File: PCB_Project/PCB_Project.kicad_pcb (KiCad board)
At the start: 4 copper layers, 53 x 30 mm, 39 parts, among them J1 Power Connector, J2 ZE27-O3, J3 i2c1, J4 i2c2, J5 SPI1, J6 SPI2, Q1 MMBT2222A, Q2 MMBT2222A

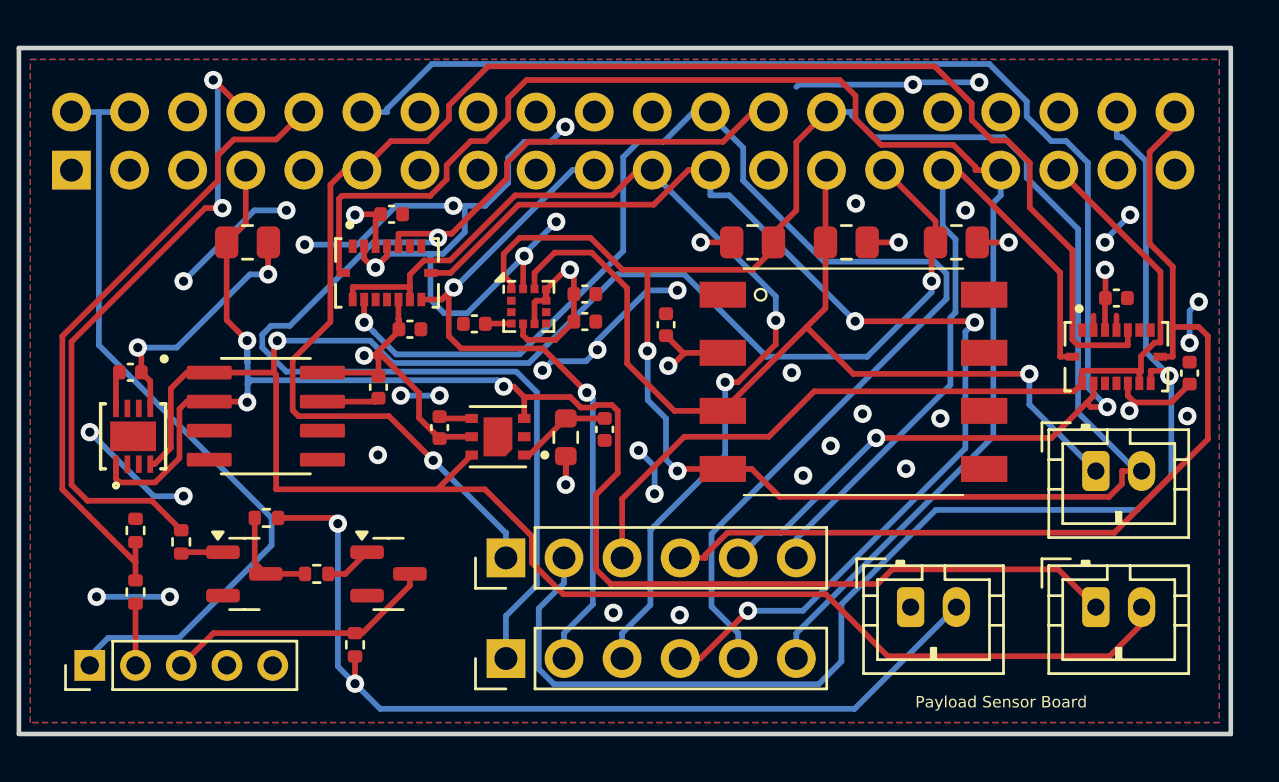
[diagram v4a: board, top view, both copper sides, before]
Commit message: added fabs and fixed i2c loop
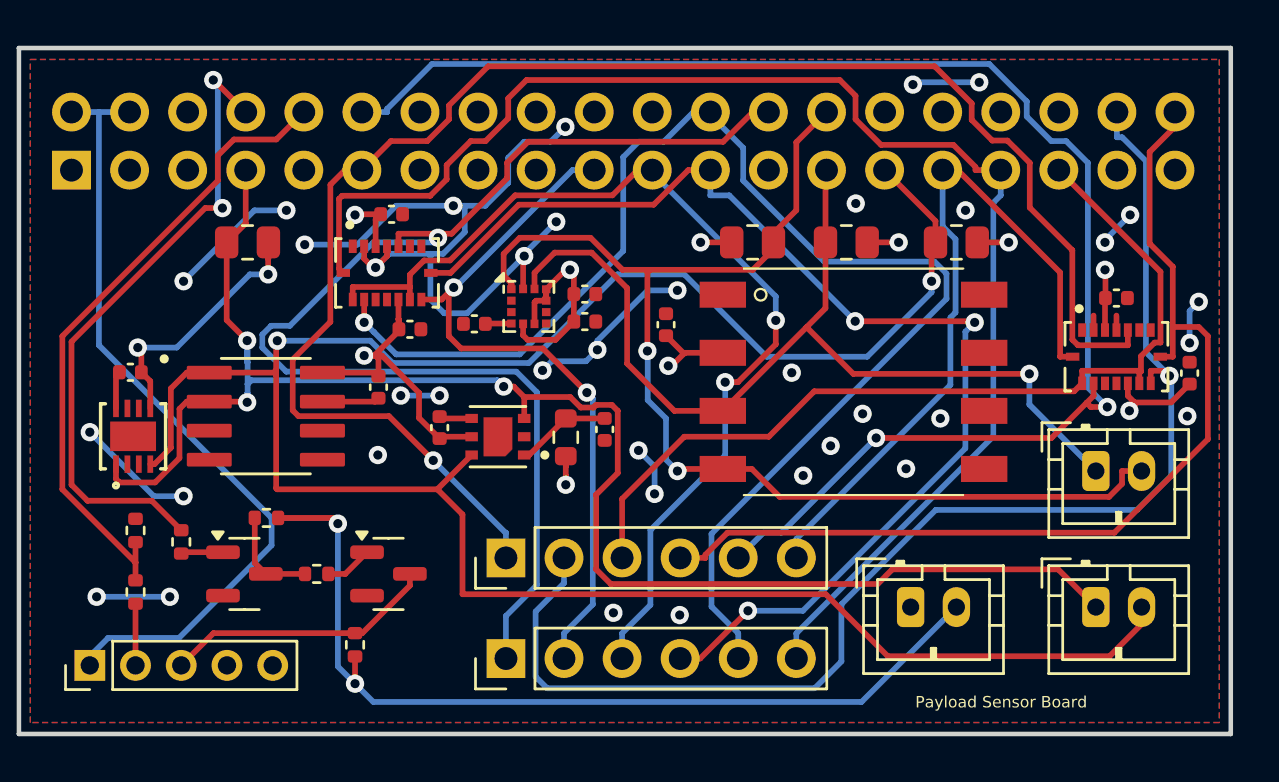
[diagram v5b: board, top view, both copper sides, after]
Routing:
- net I2C_SCL_1: track 78.3 -> 52.8 mm
- net GND: track 77.4 -> 72.3 mm
- net +3V3: track 55.4 -> 53.4 mm
- net I2C_SCL_2: track 100.3 -> 101.9 mm
- net MOSI_2: track 57.4 -> 57.9 mm

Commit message: power baby
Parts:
- removed R22, R23, R24, R25, R27: 1k, Resistor_SMD:R_0402_1005Metric
- removed R26: 2k, Resistor_SMD:R_0402_1005Metric
- added 11: LM22673MRE-5.0/NOPB, Transistor_Power:MRA08B, F.Cu at (89.6, 22.3)
- added C14: 6.8uF, Capacitor_SMD:C_1206_3216Metric, F.Cu at (96.2, 22.2)
- added C15: 1uF, Capacitor_SMD:C_0603_1608Metric, F.Cu at (93.0, 26.5)
- added D2: LED_Small, LED_SMD:LED_0805_2012Metric, F.Cu at (189.7, 84.3)
- added D3: LED_Small, LED_SMD:LED_0805_2012Metric, F.Cu at (111.8, 79.7)
- added D4: LED_Small, LED_SMD:LED_0805_2012Metric, F.Cu at (114.6, 79.7)
- added D5: LED_Small, LED_SMD:LED_0805_2012Metric, F.Cu at (117.8, 79.7)
- added D6: LED_Small, LED_SMD:LED_0805_2012Metric, F.Cu at (108.5, 79.7)
- added D7: LED_Small, LED_SMD:LED_0805_2012Metric, F.Cu at (127.8, 79.8)
- added J10: ZE27-O3, Connector_PinHeader_2.00mm:PinHeader_1x05_P2.00mm_Vertical, F.Cu at (157.1, 43.9)
- added J7: m2, Connector_JST:JST_PH_B2B-PH-K_1x02_P2.00mm_Vertical, F.Cu at (85.0, 170.2)
- added J8: m3, Connector_JST:JST_PH_B2B-PH-K_1x02_P2.00mm_Vertical, F.Cu at (96.5, 170.1)
- added J9: m4, Connector_JST:JST_PH_B2B-PH-K_1x02_P2.00mm_Vertical, F.Cu at (53.0, 170.2)
- added R10: 310, Resistor_SMD:R_0402_1005Metric, F.Cu at (185.3, 78.8)
- added R11: 310, Resistor_SMD:R_0402_1005Metric, F.Cu at (185.3, 80.8)
- added R12: 310, Resistor_SMD:R_0402_1005Metric, F.Cu at (185.3, 82.8)
- added R13: 430, Resistor_SMD:R_0402_1005Metric, F.Cu at (185.3, 84.8)
- added R14: 110, Resistor_SMD:R_0402_1005Metric, F.Cu at (161.1, 39.7)
- added R15: 1k, Resistor_SMD:R_0402_1005Metric, F.Cu at (162.4, 39.7)
- added R16: 1k, Resistor_SMD:R_0402_1005Metric, F.Cu at (164.4, 37.2)
- added R17: 1k, Resistor_SMD:R_0402_1005Metric, F.Cu at (162.1, 33.0)
- added R18: 1k, Resistor_SMD:R_0402_1005Metric, F.Cu at (157.9, 38.2)
- added R19: 2k, Resistor_SMD:R_0402_1005Metric, F.Cu at (157.9, 40.7)
- added R20: 1k, Resistor_SMD:R_0402_1005Metric, F.Cu at (111.8, 82.9)
- added R6: 1k, Resistor_SMD:R_0603_1608Metric, F.Cu at (105.3, 17.1)
- added R7: 45, Resistor_SMD:R_0603_1608Metric, F.Cu at (105.3, 19.6)
- added R9: 310, Resistor_SMD:R_0402_1005Metric, F.Cu at (185.3, 76.8)
- added U9: TPS7A5701RTER, Package_TO_SOT_SMD:WQFN16_RTE_TEX, F.Cu at (190.3, 90.8)
- C12: value 100nF -> 10nF; footprint Capacitor_SMD:C_0402_1005Metric -> Capacitor_SMD:C_0603_1608Metric
- C3: value 1µF -> 100nF
- C4: value 100nF -> 1µF
- C8: value 0.1µF -> 100nF
- J1: value Power Connector -> i2c2
- J2: value ZE27-O3 -> i2c1; footprint Connector_PinHeader_2.00mm:PinHeader_1x05_P2.00mm_Vertical -> Connector_JST:JST_PH_B2B-PH-K_1x02_P2.00mm_Vertical
- J3: value i2c1 -> SPI1; footprint Connector_JST:JST_PH_B2B-PH-K_1x02_P2.00mm_Vertical -> Connector_PinHeader_2.54mm:PinHeader_1x06_P2.54mm_Vertical
- J4: value i2c2 -> SPI2; footprint Connector_JST:JST_PH_B2B-PH-K_1x02_P2.00mm_Vertical -> Connector_PinHeader_2.54mm:PinHeader_1x06_P2.54mm_Vertical
- J5: value SPI1 -> Power Connector; footprint Connector_PinHeader_2.54mm:PinHeader_1x06_P2.54mm_Vertical -> Connector_JST:JST_PH_B2B-PH-K_1x02_P2.00mm_Vertical
- J6: value SPI2 -> m1; footprint Connector_PinHeader_2.54mm:PinHeader_1x06_P2.54mm_Vertical -> Connector_JST:JST_PH_B2B-PH-K_1x02_P2.00mm_Vertical
- U2: footprint Package_LGA:LGA-12_2x2mm_P0.5mm -> Sensor:XDCR_SGP41-D-R4
- U3: footprint Sensor:XDCR_SGP41-D-R4 -> Package_LGA:LGA-12_2x2mm_P0.5mm
- moved C7 147.0 mm to (251.9, 47.1)
- moved U6 147.0 mm to (247.0, 48.4)
- moved C5 131.4 mm to (227.7, 21.9), turned to 90 degrees
- moved R5 123.1 mm to (221.8, 19.4), turned to -90 degrees
- moved U2 123.0 mm to (224.7, 21.5)
- moved C4 122.3 mm to (220.2, 20.0), turned to 90 degrees
- moved U3 111.1 mm to (216.3, 40.2)
- moved C3 108.3 mm to (217.0, 37.8), turned to 90 degrees
- moved C1 105.4 mm to (215.2, 37.0), turned to 180 degrees
- moved C2 105.4 mm to (215.2, 38.2), turned to 180 degrees
- moved J2 105.3 mm to (190.5, 46.8)
- moved Q2 96.7 mm to (199.7, 82.8)
- moved J6 92.4 mm to (62.5, 170.4), turned to 0 degrees
- moved Q1 90.9 mm to (199.7, 78.2)
- moved J5 90.6 mm to (73.5, 170.4), turned to 0 degrees
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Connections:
- C12 pad 1: +3V3 -> Net-(11-BOOT)
- C12 pad 2: GND -> Net-(11-SW)
- C3 pad 1: Net-(U3-VDD) -> Net-(U3-C1)
- C4 pad 1: Net-(U2-C1) -> Net-(U2-VDD)
- C6 pad 1: GND -> +3V3
- C6 pad 2: +3V3 -> GND
- J1 pad 1: GND -> I2C_SDA_2
- J1 pad 2: +5V -> I2C_SCL_2
- J2 pad 1: +5V -> I2C_SDA_1
- J2 pad 2: Pi_RX_5V -> I2C_SCL_1
- J3 pad 1: I2C_SDA_1 -> CSB_Gryo_BMI088_2
- J3 pad 2: I2C_SCL_1 -> MOSI_2
- J4 pad 1: I2C_SDA_2 -> CSB_Gryo_BMI088_1
- J4 pad 2: I2C_SCL_2 -> MOSI_1
- J5 pad 1: CSB_Gryo_BMI088_2 -> GND
- J5 pad 2: MOSI_2 -> BATTV
- J6 pad 1: CSB_Gryo_BMI088_1 -> GND
- J6 pad 2: MOSI_1 -> S1
- R5 pad 2: Net-(U3-VDD) -> Net-(U2-VDD)
- U2 pad 1: I2C_SCL_1 -> Net-(U2-VDD)
- U2 pad 3: GND -> I2C_SDA_2
- U2 pad 4: Net-(U2-C1) -> GND
- U2 pad 6: +3V3 -> I2C_SCL_2
- U2 pad 7: unconnected-(U2-Int-Pad7) -> GND
- U3 pad 1: Net-(U3-VDD) -> I2C_SCL_1
- U3 pad 3: I2C_SDA_2 -> GND
- U3 pad 4: GND -> Net-(U3-C1)
- U3 pad 6: I2C_SCL_2 -> +3V3
- U3 pad 7: GND -> unconnected-(U3-Int-Pad7)
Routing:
- net I2C_SCL_2: track 101.9 -> 0.00 mm, vias 2 -> 0
- net +5V: track 77.7 -> 0.00 mm, vias 2 -> 0
- net GND: track 72.3 -> 0.00 mm, vias 31 -> 0
- net CSB_Gryo_BMI088_2: track 70.2 -> 0.00 mm, vias 1 -> 0
- net I2C_SDA_2: track 69.7 -> 0.00 mm, vias 3 -> 0
- net CSB_Accel_BMI088_2: track 65.9 -> 0.00 mm, vias 2 -> 0
- net BMI088_INT1_1: track 62.7 -> 0.00 mm
- net CSB_Accel_BMI088_1: track 59.3 -> 0.00 mm, vias 1 -> 0
- net MOSI_2: track 57.9 -> 0.00 mm, vias 1 -> 0
- net CSB_Gryo_BMI088_1: track 54.5 -> 0.00 mm, vias 1 -> 0
- net +3V3: track 53.4 -> 0.00 mm, vias 18 -> 0
- net I2C_SCL_1: track 52.8 -> 0.00 mm, vias 2 -> 0
- net SCK_1: track 51.0 -> 0.00 mm, vias 3 -> 0
- net SCK_2: track 43.6 -> 0.00 mm
- net MISO_1: track 43.6 -> 0.00 mm, vias 2 -> 0
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- added copper zone on B.Cu, net BATTV
- removed copper zone on B.Cu, net +3V3
- removed copper zone on In2.Cu, net +3V3
- removed copper zone on F.Cu, net GND
- removed copper zone on In1.Cu, net GND
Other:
- board size 53 x 30 mm -> 70 x 70 mm
- board text added: "1"
- board text added: "2"
- board text added: "3"
- board text added: "4"
- board text added: "5V"
- board text added: "BATT"
- board text added: "STARR"
- board text removed: "Payload Sensor Board"

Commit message: finally
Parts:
- removed 11: LM22673MRE-5.0/NOPB, Transistor_Power:MRA08B
- removed J7: m2, Connector_JST:JST_PH_B2B-PH-K_1x02_P2.00mm_Vertical
- removed J8: m3, Connector_JST:JST_PH_B2B-PH-K_1x02_P2.00mm_Vertical
- removed J9: m4, Connector_JST:JST_PH_B2B-PH-K_1x02_P2.00mm_Vertical
- removed R10, R11: 310, Resistor_SMD:R_0402_1005Metric
- removed R14: 110, Resistor_SMD:R_0402_1005Metric
- removed U9: TPS7A5701RTER, Package_TO_SOT_SMD:WQFN16_RTE_TEX
- added 111: LM22673MRE-5.0/NOPB, Transistor_Power:MRA08B, F.Cu at (112.0, 85.9)
- added 1111: LM22673MRE-5.0/NOPB, Transistor_Power:MRA08B, B.Cu at (102.6, 85.6)
- added 11111: LM22673MRE-5.0/NOPB, Transistor_Power:MRA08B, B.Cu at (122.4, 85.7)
- added 11112: LM22673MRE-5.0/NOPB, Transistor_Power:MRA08B, F.Cu at (146.6, 97.4)
- added 11113: LM22673MRE-5.0/NOPB, Transistor_Power:MRA08B, B.Cu at (140.9, 85.7)
- added 11114: LM22673MRE-5.0/NOPB, Transistor_Power:MRA08B, B.Cu at (161.3, 85.8)
- added C13: 100uF, Capacitor_SMD:CP_WCAP-PSHP, B.Cu at (108.5, 72.8)
- added C16: 100uF, Capacitor_SMD:CP_WCAP-PSHP, F.Cu at (113.8, 97.5)
- added C17: 6.8uF, Capacitor_SMD:C_1206_3216Metric, F.Cu at (112.0, 91.2)
- added C18: 1uF, Capacitor_SMD:C_0603_1608Metric, B.Cu at (98.4, 82.3)
- added C19: 120uF, Capacitor_SMD:CP_Elec_10x12.5, B.Cu at (113.2, 96.0)
- added C20: 1uF, Capacitor_SMD:C_0603_1608Metric, F.Cu at (107.8, 89.0)
- added C21: 120uF, Capacitor_SMD:CP_Elec_10x12.5, F.Cu at (119.5, 76.0)
- added C22: 10nF, Capacitor_SMD:C_0603_1608Metric, B.Cu at (126.5, 85.8)
- added C23: 100uF, Capacitor_SMD:CP_WCAP-PSHP, B.Cu at (124.0, 72.0)
- added C24: 6.8uF, Capacitor_SMD:C_1206_3216Metric, B.Cu at (122.4, 80.2)
- added C25: 1uF, Capacitor_SMD:C_0603_1608Metric, B.Cu at (118.2, 82.5)
- added C26: 120uF, Capacitor_SMD:CP_Elec_10x12.5, B.Cu at (132.4, 95.2)
- added C27: 10nF, Capacitor_SMD:C_0603_1608Metric, F.Cu at (146.7, 93.5)
- added C28: 100uF, Capacitor_SMD:CP_WCAP-PSHP, F.Cu at (161.0, 94.8)
- added C29: 6.8uF, Capacitor_SMD:C_1206_3216Metric, F.Cu at (152.0, 97.2)
- added C30: 1uF, Capacitor_SMD:C_0603_1608Metric, F.Cu at (149.8, 101.5)
- added C31: 120uF, Capacitor_SMD:CP_Elec_10x12.5, F.Cu at (137.2, 88.8)
- added C32: 10nF, Capacitor_SMD:C_0603_1608Metric, B.Cu at (145.3, 85.8)
- added C33: 100uF, Capacitor_SMD:CP_WCAP-PSHP, B.Cu at (147.3, 72.0)
- added C34: 6.8uF, Capacitor_SMD:C_1206_3216Metric, B.Cu at (141.0, 80.3)
- added C35: 1uF, Capacitor_SMD:C_0603_1608Metric, B.Cu at (136.8, 82.5)
- added C36: 120uF, Capacitor_SMD:CP_Elec_10x12.5, B.Cu at (151.2, 95.3)
- added C37: 10nF, Capacitor_SMD:C_0603_1608Metric, B.Cu at (165.6, 85.7)
- added C38: 100uF, Capacitor_SMD:CP_WCAP-PSHP, B.Cu at (164.2, 71.2)
- added C39: 6.8uF, Capacitor_SMD:C_1206_3216Metric, B.Cu at (161.3, 80.3)
- added C40: 1uF, Capacitor_SMD:C_0603_1608Metric, B.Cu at (157.1, 82.5)
- added C41: 120uF, Capacitor_SMD:CP_Elec_10x12.5, B.Cu at (171.5, 95.3)
- added D1: 60V, 5A, Diode_SMD:D_PowerDI-5, B.Cu at (112.9, 79.6)
- added D10: 60V, 5A, Diode_SMD:D_PowerDI-5, B.Cu at (171.6, 79.2)
- added D11: LED_Small, Diode_SMD:D_0603_1608Metric, F.Cu at (160.2, 73.2)
- added D12: LED_Small, Diode_SMD:D_0603_1608Metric, F.Cu at (157.2, 73.2)
- added D13: LED_Small, Diode_SMD:D_0603_1608Metric, F.Cu at (154.0, 73.2)
- added D8: LED_Small, Diode_SMD:D_0603_1608Metric, F.Cu at (166.2, 73.2)
- added D9: LED_Small, Diode_SMD:D_0603_1608Metric, F.Cu at (163.2, 73.2)
- added H1: MountingHole_Pad, MountingHole:MountingHole_2.5mm_Pad, F.Cu at (99.6, 64.2)
- added H2: MountingHole_Pad, MountingHole:MountingHole_2.5mm_Pad, F.Cu at (157.6, 64.2)
- added H3: MountingHole_Pad, MountingHole:MountingHole_2.5mm_Pad, F.Cu at (99.6, 106.3)
- added H4: MountingHole_Pad, MountingHole:MountingHole_2.5mm_Pad, F.Cu at (157.6, 106.3)
- added J11: ZE27-O3, Connector_PinHeader_2.00mm:PinHeader_1x05_P2.00mm_Vertical, F.Cu at (98.8, 80.0)
- added J12: Conn_01x03_Socket, Connector_JST:JST_PH_B3B-PH-K_1x03_P2.00mm_Vertical, F.Cu at (105.8, 105.7)
- added J13: Conn_01x03_Socket, Connector_JST:JST_PH_B3B-PH-K_1x03_P2.00mm_Vertical, F.Cu at (138.8, 105.7)
- added J14: Conn_01x03_Socket, Connector_JST:JST_PH_B3B-PH-K_1x03_P2.00mm_Vertical, F.Cu at (148.1, 105.7)
- added L1: 6uH, Inductor_SMD:L_6.7x6.7mm, B.Cu at (111.5, 85.2)
- added L2: 6uH, Inductor_SMD:L_6.7x6.7mm, F.Cu at (120.5, 86.0)
- added L3: 6uH, Inductor_SMD:L_6.7x6.7mm, B.Cu at (131.0, 85.5)
- added L4: 6uH, Inductor_SMD:L_6.7x6.7mm, F.Cu at (147.0, 89.0)
- added L5: 6uH, Inductor_SMD:L_6.7x6.7mm, B.Cu at (150.0, 85.2)
- added L6: 6uH, Inductor_SMD:L_6.7x6.7mm, B.Cu at (170.3, 85.8)
- added R21: 1k, Resistor_SMD:R_0402_1005Metric, F.Cu at (101.8, 76.0)
- added R22: 1k, Resistor_SMD:R_0402_1005Metric, F.Cu at (105.7, 76.2)
- added R23: 1k, Resistor_SMD:R_0402_1005Metric, F.Cu at (110.2, 72.0)
- added R24: 2k, Resistor_SMD:R_0402_1005Metric, F.Cu at (105.8, 78.5)
- added R25: 1k, Resistor_SMD:R_0402_1005Metric, F.Cu at (103.3, 78.5)
- added R8: 45, Resistor_SMD:R_0603_1608Metric, F.Cu at (108.6, 79.2)
- C12, C14: moved to B.Cu
- C15: value 1uF -> 10nF
- D2: value LED_Small -> 15.6V, >3A; footprint LED_SMD:LED_0805_2012Metric -> Diode_SMD:D_PowerDI-5
- D3, D5: value LED_Small -> 60V, 5A; footprint LED_SMD:LED_0805_2012Metric -> Diode_SMD:D_PowerDI-5; moved to B.Cu
- D4: value LED_Small -> 60V, 5A; footprint LED_SMD:LED_0805_2012Metric -> Diode_SMD:D_PowerDI-5
- D6, D7: footprint LED_SMD:LED_0805_2012Metric -> Diode_SMD:D_0603_1608Metric
- J1: value i2c2 -> SPI1; footprint Connector_JST:JST_PH_B2B-PH-K_1x02_P2.00mm_Vertical -> Connector_PinHeader_2.54mm:PinHeader_1x06_P2.54mm_Vertical
- J10: value ZE27-O3 -> Motor Power Connection; footprint Connector_PinHeader_2.00mm:PinHeader_1x05_P2.00mm_Vertical -> Connector_JST:JST_PH_B2B-PH-K_1x02_P2.00mm_Vertical
- J2: value i2c1 -> i2c2
- J3: value SPI1 -> i2c1; footprint Connector_PinHeader_2.54mm:PinHeader_1x06_P2.54mm_Vertical -> Connector_JST:JST_PH_B2B-PH-K_1x02_P2.00mm_Vertical
- J5: value Power Connector -> Battery Connector
- J6: value m1 -> Conn_01x03_Socket; footprint Connector_JST:JST_PH_B2B-PH-K_1x02_P2.00mm_Vertical -> Connector_JST:JST_PH_B3B-PH-K_1x03_P2.00mm_Vertical
- R12: value 310 -> 200
- R13: value 430 -> 200
- R15, R16, R17: value 1k -> 200
- R18: value 1k -> 800
- R19: value 2k -> 200
- R6: value 1k -> 10k; footprint Resistor_SMD:R_0603_1608Metric -> Resistor_SMD:R_0402_1005Metric
- R7: value 45 -> 1k
- R9: value 310 -> 10k
- U3: footprint Package_LGA:LGA-12_2x2mm_P0.5mm -> Sensor:XDCR_LIS3MDL
- U4: footprint Sensor:HNNJ footprint -> Sensor:HNNJ
- U6: footprint Sensor:SOIC127P600X175-8N -> Sensor:SOIC-8
- moved J1 109.0 mm to (98.7, 97.9), turned to 180 degrees
- moved Q1 97.2 mm to (102.7, 73.3), turned to 180 degrees
- moved C1 96.6 mm to (128.9, 80.2), turned to -90 degrees
- moved R6 96.5 mm to (169.0, 89.5), turned to 90 degrees
- moved C2 94.9 mm to (130.2, 80.2), turned to -90 degrees
- moved R1 94.2 mm to (115.0, 68.2)
- moved C3 93.9 mm to (131.8, 77.0)
- moved Q2 93.5 mm to (106.8, 73.1), turned to -90 degrees
- moved C8 93.2 mm to (174.6, 62.0), turned to 0 degrees
- moved R4 92.7 mm to (141.2, 68.2), turned to 0 degrees
- moved U3 92.7 mm to (132.3, 79.5), turned to -90 degrees
- moved U1 92.7 mm to (104.5, 65.2)
- moved R3 92.5 mm to (131.9, 68.2)
- moved R2 92.3 mm to (136.2, 68.2), turned to 180 degrees
- moved J4 91.8 mm to (179.3, 63.5)
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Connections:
- C15 pad 2: GND -> Net-(111-SW)
- D2 pad 1: GND -> Net-(111-SW)
- D2 pad 2: Net-(D2-A) -> GND
- D3 pad 1: GND -> Net-(11111-SW)
- D3 pad 2: Net-(D3-A) -> GND
- D4 pad 1: GND -> Net-(11112-SW)
- D4 pad 2: Net-(D4-A) -> GND
- D5 pad 1: GND -> Net-(11113-SW)
- D5 pad 2: Net-(D5-A) -> GND
- J1 pad 1: I2C_SDA_2 -> CSB_Gryo_BMI088_2
- J1 pad 2: I2C_SCL_2 -> MOSI_2
- J10 pad 1: +5V -> M1
- J10 pad 2: Pi_RX_5V -> GND
- J2 pad 1: I2C_SDA_1 -> I2C_SDA_2
- J2 pad 2: I2C_SCL_1 -> I2C_SCL_2
- J3 pad 1: CSB_Gryo_BMI088_2 -> I2C_SDA_1
- J3 pad 2: MOSI_2 -> I2C_SCL_1
- J5 pad 1: GND -> BATTV
- J5 pad 2: BATTV -> GND
- J6 pad 1: GND -> S2_PWM
- J6 pad 2: S1 -> S2
- R12 pad 1: Net-(D5-A) -> Net-(D6-A)
- R12 pad 2: S4 -> M1
- R13 pad 1: Net-(D6-A) -> Net-(D7-A)
- R13 pad 2: BATTV -> S1
- R15 pad 1: Net-(Q2-C) -> Net-(D8-A)
- R15 pad 2: +5V -> S2
- R16 pad 1: Pi_TX_5V -> Net-(D9-A)
- R16 pad 2: +5V -> S3
- R17 pad 1: Net-(Q2-C) -> Net-(D11-A)
- R17 pad 2: Net-(Q1-B) -> S4
- R18 pad 1: Net-(Q2-B) -> Net-(D12-A)
- R18 pad 2: Pi_TX -> BATTV
- R19 pad 1: GND -> Net-(D13-A)
- R19 pad 2: Pi_RX -> +5.25V
- R20 pad 1: Pi_RX -> Net-(Q2-C)
- R20 pad 2: Pi_RX_5V -> +5.25V
- R6 pad 1: Net-(11-FB) -> GND
- R6 pad 2: GND -> Net-(U6-CT)
- R7 pad 1: Net-(11-FB) -> Net-(111-FB)
- R7 pad 2: +5V5 -> GND
- R9 pad 1: Net-(D2-A) -> ADT_INT
- R9 pad 2: S1 -> GND
- U1 pad 13: unconnected-(U1-GPIO_27-Pad13) -> S3_PWM
- U1 pad 15: unconnected-(U1-GPIO_22-Pad15) -> S4_PWM
- U1 pad 16: unconnected-(U1-GPIO_23-Pad16) -> S1_PWM
- U1 pad 18: unconnected-(U1-GPIO_24-Pad18) -> S2_PWM
- U1 pad 2: +5V -> +5.25V
- U1 pad 32: unconnected-(U1-GPIO_12-Pad32) -> ADT_INT
- U1 pad 4: +5V -> +5.25V
- U6 pad 5: unconnected-(U6-INT-Pad5) -> ADT_INT
- U6 pad 6: unconnected-(U6-CT-Pad6) -> Net-(U6-CT)
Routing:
- net S1: track 0.00 -> 106.9 mm, vias 0 -> 1
- net I2C_SDA_2: track 0.00 -> 104.1 mm
- net I2C_SCL_1: track 0.00 -> 100.9 mm, vias 0 -> 1
- net S2: track 0.00 -> 99.6 mm, vias 0 -> 1
- net I2C_SDA_1: track 0.00 -> 99.3 mm, vias 0 -> 1
- net +5.25V: track 0.00 -> 96.5 mm, vias 0 -> 5
- net M1: track 0.00 -> 89.7 mm, vias 0 -> 1
- net I2C_SCL_2: track 0.00 -> 82.8 mm
- net S3: track 0.00 -> 82.3 mm, vias 0 -> 1
- net SCK_2: track 0.00 -> 76.9 mm, vias 0 -> 1
- net S4: track 0.00 -> 76.9 mm, vias 0 -> 1
- net MOSI_2: track 0.00 -> 75.0 mm
- net MISO_2: track 0.00 -> 72.6 mm
- net BMI088_INT1_2: track 0.00 -> 71.2 mm
- net CSB_Gryo_BMI088_2: track 0.00 -> 70.9 mm
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- added copper zone on In1.Cu, net +3V3
- added copper zone on In1.Cu, net +5.25V
- added copper zone on F.Cu, net BATTV
- added copper zone on In2.Cu, net BATTV
- added copper zone on B.Cu, net GND
- added copper zone on F.Cu, net GND
- added copper zone on F.Cu, net Net-(111-SW)
- added copper zone on B.Cu, net Net-(1111-SW)
- added copper zone on B.Cu, net Net-(11111-SW)
- added copper zone on F.Cu, net Net-(11112-SW)
- added copper zone on B.Cu, net Net-(11113-SW)
- added copper zone on B.Cu, net Net-(11114-SW)
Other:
- board size 70 x 70 mm -> 86 x 49 mm
- board text added: "I2C1"
- board text added: "I2C2"
- board text added: "M1"
- board text added: "S1"
- board text added: "S2"
- board text added: "S3"
- board text added: "S4"
- board text added: "STARR Payload"
- board text removed: "1"
- board text removed: "2"
- board text removed: "3"
- board text removed: "4"
- board text removed: "STARR"

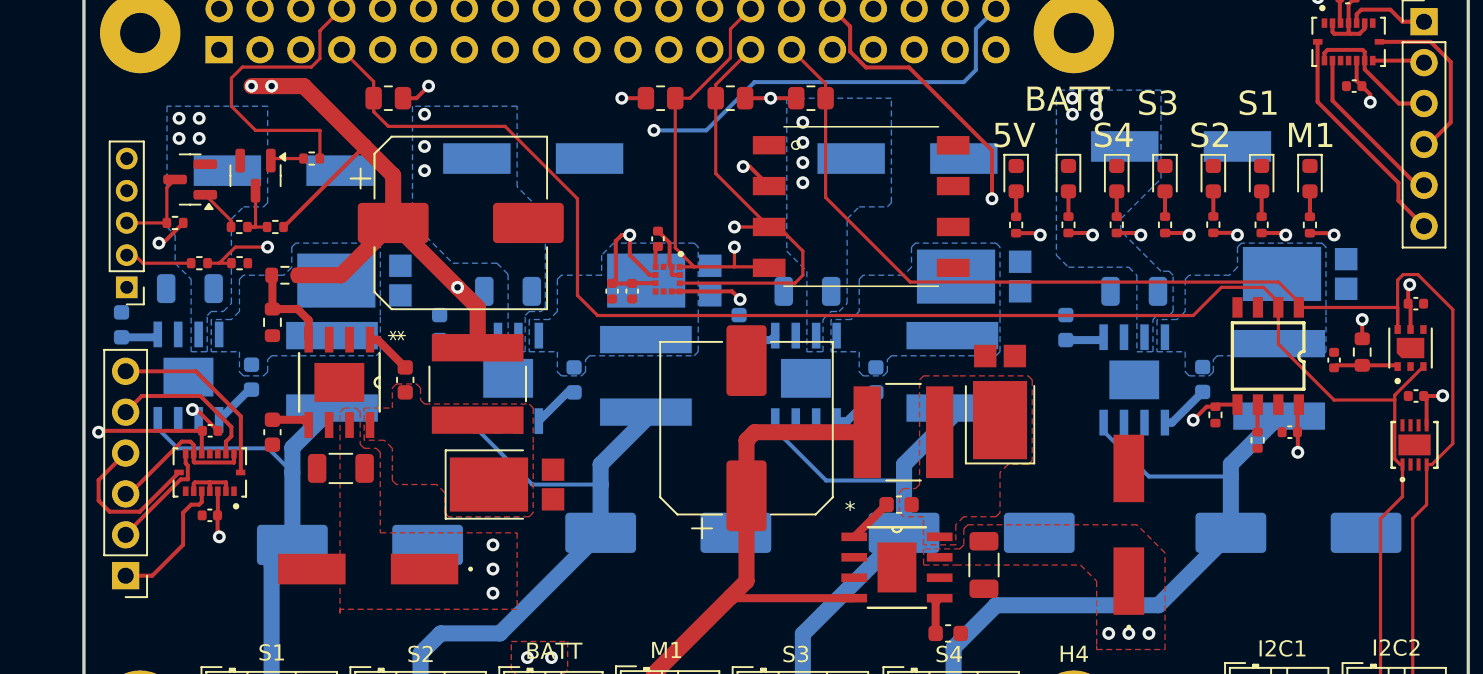
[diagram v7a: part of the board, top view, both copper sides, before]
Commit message: Cleaned up wiring, Fixed missing BATTV connection
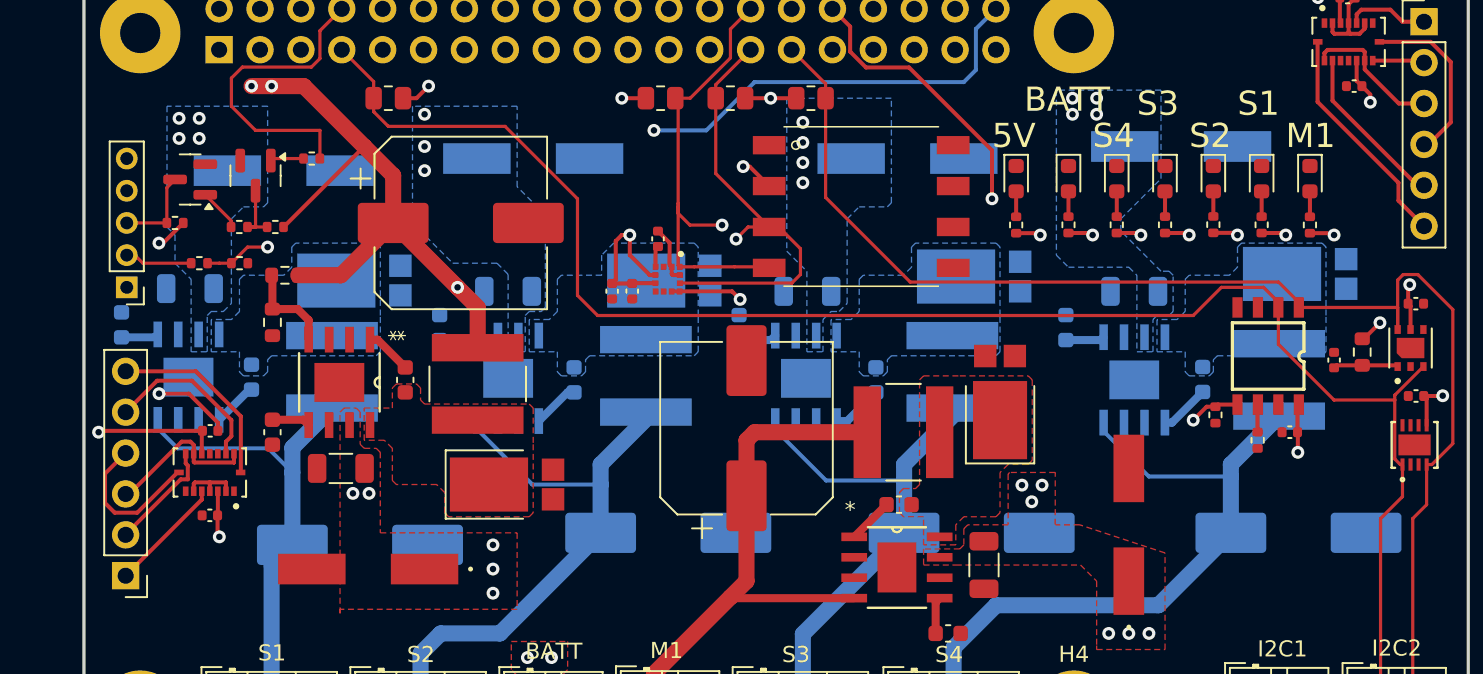
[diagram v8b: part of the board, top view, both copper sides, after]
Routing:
- net CSB_Accel_BMI088_2: track 42.4 -> 46.6 mm
- net GND: track 14.8 -> 17.6 mm
- net CSB_Gryo_BMI088_2: track 70.9 -> 69.2 mm
- net Pi_RX: track 22.7 -> 21.9 mm
- net I2C_SDA_1: track 99.3 -> 99.8 mm
- net BATTV: vias 24 -> 29
